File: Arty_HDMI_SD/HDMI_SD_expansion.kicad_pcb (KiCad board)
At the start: 2 copper layers, 109 x 40 mm, 54 parts, among them J1 0015912120, J2 1140084168, J3 0015912120, J4 2000-1-2-41-00-BK, J5 UE27AC54100, J6 0015912120, U1 TPS61232DRCT, U2 MAX3421EEHJ, Y1 KX-7_12,MHz

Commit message: PCB routing
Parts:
- removed G***: LOGO, antmicro-footprints:antmicro-logo_scaled_30mm
- added N1: antmicro_logo, antmicro-footprints:antmicro-logo_scaled_30mm, F.Cu at (165.8, 92.9)
- moved R2 104.2 mm to (196.6, 115.9), turned to 270 degrees
- moved R7 99.6 mm to (194.3, 115.9), turned to 270 degrees
- moved J4 97.5 mm to (98.3, 95.3), turned to 90 degrees
- moved J2 95.8 mm to (194.1, 104.5), turned to 90 degrees
- moved R1 95.0 mm to (192.1, 115.9), turned to 270 degrees
- moved J5 91.0 mm to (101.4, 114.5), turned to 270 degrees
- moved R12 90.9 mm to (190.1, 116.1), turned to 90 degrees
- moved C1 78.8 mm to (186.2, 104.7), turned to 180 degrees
- moved D1 77.2 mm to (107.7, 114.2), turned to 90 degrees
- moved C19 77.2 mm to (110.5, 118.0), turned to 180 degrees
- moved C18 76.2 mm to (110.5, 116.5), turned to 180 degrees
- moved D2 76.0 mm to (107.7, 111.6), turned to 270 degrees
- moved R10 74.3 mm to (110.7, 112.1), turned to 0 degrees
- moved C16 73.8 mm to (112.7, 120.1), turned to 90 degrees
- moved C15 73.7 mm to (109.4, 106.8), turned to 0 degrees
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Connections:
- net Net-(D1-Pad2) renamed /Data+
- net Net-(D2-Pad2) renamed /Data-
- net Net-(R10-Pad2) renamed /D+
- net Net-(R9-Pad2) renamed /D-
- J3 pad 1: /TDMS_D2_P -> /TDMS_D0_P
- J3 pad 2: /TDMS_D0_P -> /TDMS_D2_P
- J3 pad 3: /TDMS_D2_N -> /TDMS_D0_N
- J3 pad 4: /TDMS_D0_N -> /TDMS_D2_N
- J3 pad 5: /TDMS_CLK_P -> /TDMS_D1_P
- J3 pad 6: /TDMS_D1_P -> /TDMS_CLK_P
- J3 pad 7: /TDMS_CLK_N -> /TDMS_D1_N
- J3 pad 8: /TDMS_D1_N -> /TDMS_CLK_N
- J4 pad 13: /NC -> Net-(J4-Pad13)
- J4 pad 14: /NC -> Net-(J4-Pad14)
- J4 pad 15: /NC -> Net-(J4-Pad15)
- J4 pad 16: /NC -> Net-(J4-Pad16)
- J4 pad 18: /NC -> Net-(J4-Pad18)
- J4 pad 19: /NC -> Net-(J4-Pad19)
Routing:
- net /TDMS_CLK_N: track 0.00 -> 79.7 mm, vias 0 -> 1
- net /TDMS_CLK_P: track 0.00 -> 79.7 mm, vias 0 -> 1
- net /TDMS_D2_P: track 0.00 -> 79.4 mm, vias 0 -> 1
- net /TDMS_D2_N: track 0.00 -> 79.3 mm, vias 0 -> 1
- net GND: track 0.00 -> 78.9 mm, vias 0 -> 27
- net /TDMS_D0_P: track 0.00 -> 78.7 mm, vias 0 -> 1
- net /TDMS_D0_N: track 0.00 -> 78.6 mm, vias 0 -> 1
- net /TDMS_D1_P: track 0.00 -> 77.1 mm, vias 0 -> 1
- net /TDMS_D1_N: track 0.00 -> 77.1 mm, vias 0 -> 1
- net /INT_USB: track 0.00 -> 47.6 mm, vias 0 -> 1
- net /DAT2: track 0.00 -> 43.6 mm, vias 0 -> 2
- net +3V3: track 0.00 -> 40.5 mm, vias 0 -> 13
- net /DAT1: track 0.00 -> 38.2 mm
- net /CD_DAT3: track 0.00 -> 35.3 mm
- net /MOSI_CMD: track 0.00 -> 31.9 mm
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- added copper zone on In2.Cu, net +3V3
- added copper zone on In1.Cu, net GND
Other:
- copper layers 2 -> 4
- net class Default: clearance 0.2 -> 0.15; trace_width 0.25 -> 0.254; via_dia 0.8 -> 0.6; via_drill 0.4 -> 0.25
- rule trace_clearance: 0.2 -> 0.15
- rule trace_min: 0.2 -> 0.1
- rule via_min_drill: 0.3 -> 0.2
- rule via_min_size: 0.4 -> 0.2
- board text added: "Arty expansion board"
- board text added: "Rev.1.0 09/2019"

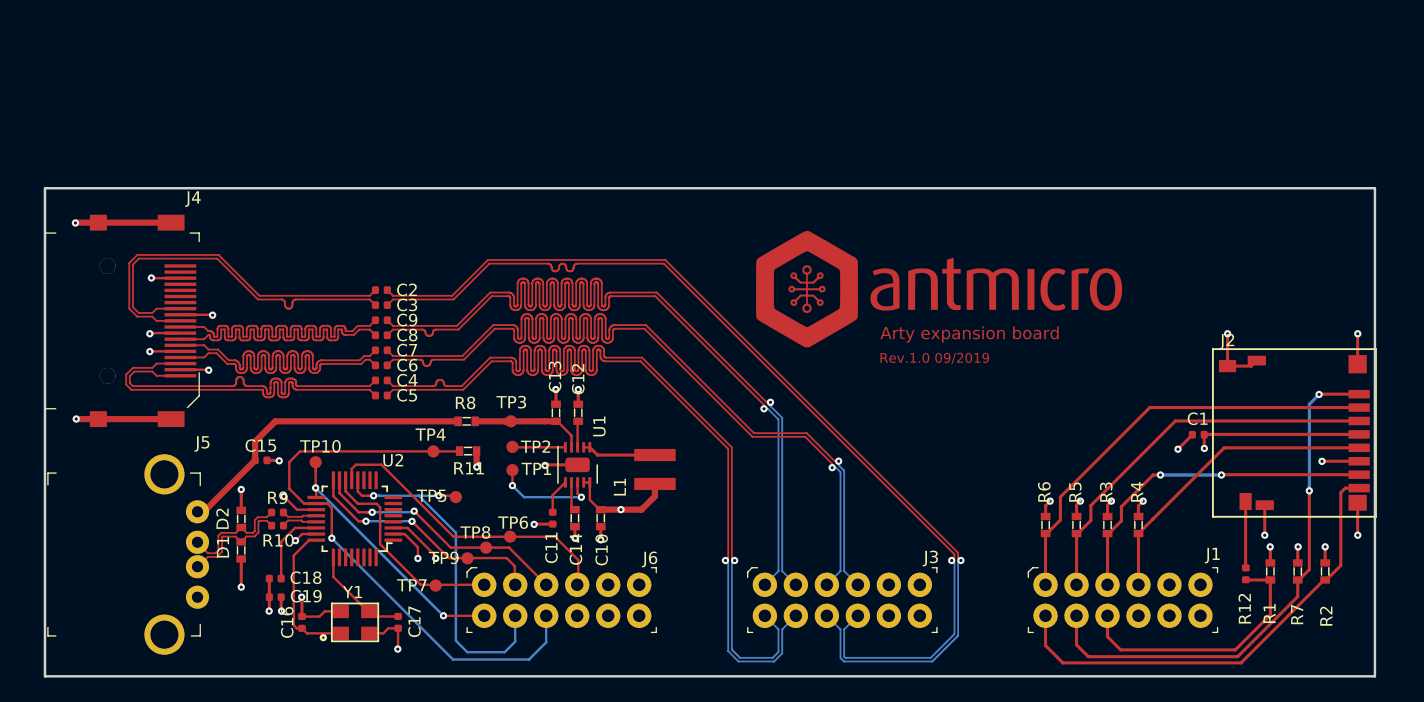
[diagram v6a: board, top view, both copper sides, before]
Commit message: Updated PMOD connectors on PCB
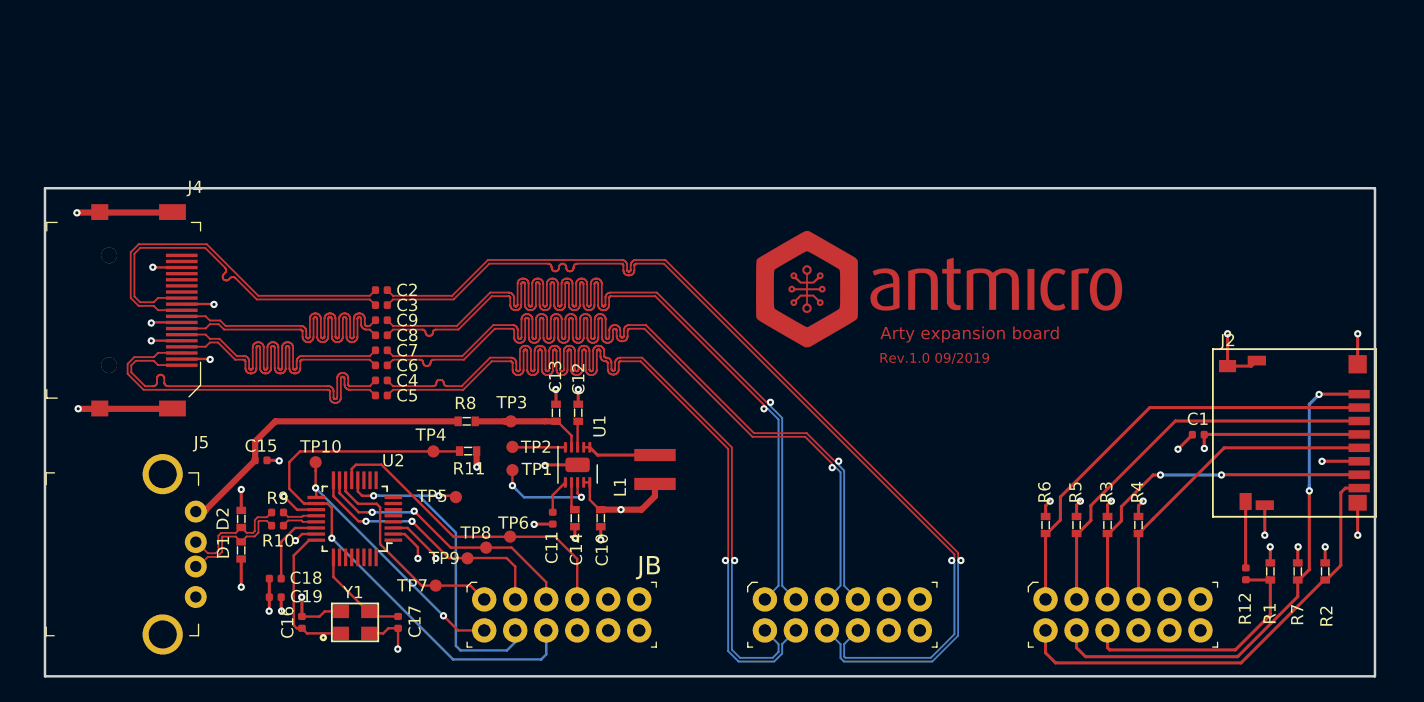
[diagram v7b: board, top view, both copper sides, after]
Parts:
- moved JB1 1.20 mm to (127.7, 118.0)
- moved JC1 1.20 mm to (150.7, 118.0)
- moved JD1 1.20 mm to (173.7, 118.0)
- moved J4 0.88 mm to (98.4, 94.5)
- moved J5 0.14 mm to (101.3, 114.5)
- renumbered J6 to JB1, J3 to JC1, J1 to JD1
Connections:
- JB1 pad 10: GND -> Net-(JB1-Pad10)
- JB1 pad 11: +3V3 -> GND
- JB1 pad 2: /GPX_USB -> /MOSI_USB
- JB1 pad 3: /MOSI_USB -> /MISO_USB
- JB1 pad 4: /RST_USB -> /SCK_USB
- JB1 pad 5: /MISO_USB -> GND
- JB1 pad 6: /INT_USB -> +3V3
- JB1 pad 7: /SCK_USB -> /GPX_USB
- JB1 pad 8: Net-(J6-Pad8) -> /RST_USB
- JB1 pad 9: GND -> /INT_USB
- JC1 pad 10: GND -> /TDMS_CLK_N
- JC1 pad 11: +3V3 -> GND
- JC1 pad 2: /TDMS_D2_P -> /TDMS_D0_N
- JC1 pad 3: /TDMS_D0_N -> /TDMS_D1_P
- JC1 pad 4: /TDMS_D2_N -> /TDMS_D1_N
- JC1 pad 5: /TDMS_D1_P -> GND
- JC1 pad 6: /TDMS_CLK_P -> +3V3
- JC1 pad 7: /TDMS_D1_N -> /TDMS_D2_P
- JC1 pad 8: /TDMS_CLK_N -> /TDMS_D2_N
- JC1 pad 9: GND -> /TDMS_CLK_P
- JD1 pad 10: GND -> /NC_EN
- JD1 pad 11: +3V3 -> GND
- JD1 pad 2: /DAT1 -> /MOSI_CMD
- JD1 pad 3: /MOSI_CMD -> /MISO_DAT0
- JD1 pad 4: /DAT2 -> /SCK
- JD1 pad 5: /MISO_DAT0 -> GND
- JD1 pad 6: /CD -> +3V3
- JD1 pad 7: /SCK -> /DAT1
- JD1 pad 8: /NC_EN -> /DAT2
- JD1 pad 9: GND -> /CD
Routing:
- net /TDMS_D1_N: track 77.1 -> 79.8 mm
- net /TDMS_D1_P: track 77.1 -> 79.9 mm
- net /MISO_USB: track 21.2 -> 22.5 mm
- net /MOSI_CMD: track 31.9 -> 33.1 mm
- net /MISO_DAT0: track 27.5 -> 28.7 mm
- net /TDMS_D0_P: track 78.7 -> 79.9 mm
- net /TDMS_D0_N: track 78.6 -> 79.8 mm
- net /SCK: track 25.2 -> 26.4 mm
- net /CD_DAT3: track 35.3 -> 36.5 mm
- net /MOSI_USB: track 20.1 -> 21.3 mm
- net /SCK_USB: track 24.9 -> 26.1 mm
- net /RST_USB: track 30.1 -> 29.0 mm
- net /DAT2: track 43.6 -> 42.5 mm
- net /DAT1: track 38.2 -> 37.3 mm
- net /INT_USB: track 47.6 -> 47.0 mm
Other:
- board text added: "JB"

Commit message: Bug Fix
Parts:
- moved C11 0.75 mm to (133.3, 110.8)
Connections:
- J5 pad SH: Net-(J5-PadSH) -> GND
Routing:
- net Net-(C12-Pad1): track 13.8 -> 29.6 mm
- net Net-(C11-Pad1): track 2.88 -> 2.13 mm
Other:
- board text added: "JC"
- board text added: "JD"
